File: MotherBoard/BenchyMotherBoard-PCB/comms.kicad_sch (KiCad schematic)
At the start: 9 parts, among them J18 COMMS-PWR, J19 COMMS-ELOAD, J20 COMMS-SWITCHER, J21 RELAYS-CONN, J22 COMMS-LOGIC

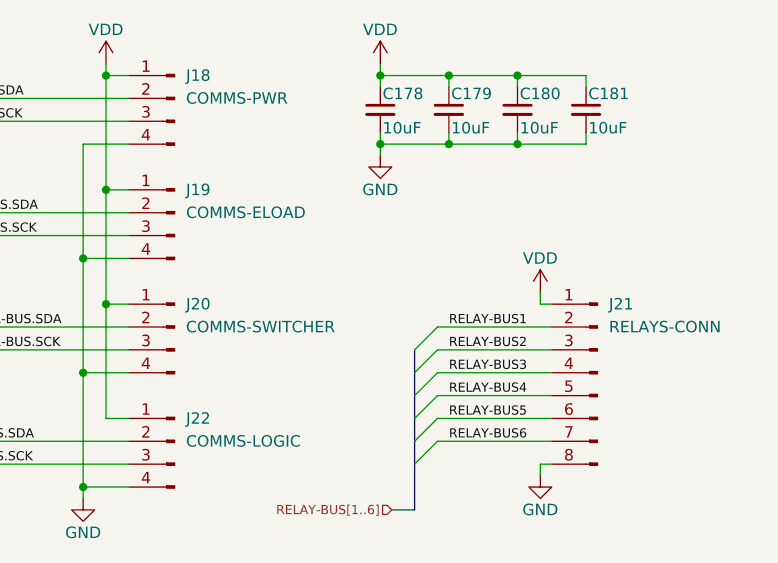
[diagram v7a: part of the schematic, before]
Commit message: Initial DDR routing, start fixing skew
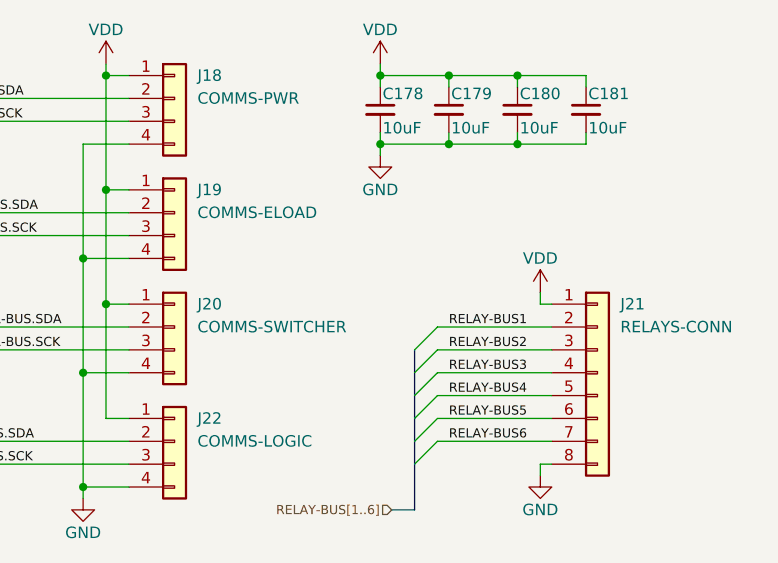
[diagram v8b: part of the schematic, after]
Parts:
- removed J18: COMMS-PWR, Daxxn_Connectors:JST_XH_B4B-XH-A_Vertical, symbol Connector:Conn_01x04_Male
- removed J19: COMMS-ELOAD, Daxxn_Connectors:JST_XH_B4B-XH-A_Vertical, symbol Connector:Conn_01x04_Male
- removed J20: COMMS-SWITCHER, Daxxn_Connectors:JST_XH_B4B-XH-A_Vertical, symbol Connector:Conn_01x04_Male
- removed J21: RELAYS-CONN, Connector_JST:JST_XH_B8B-XH-A_1x08_P2.50mm_Vertical, symbol Connector:Conn_01x08_Male
- removed J22: COMMS-LOGIC, Daxxn_Connectors:JST_XH_B4B-XH-A_Vertical, symbol Connector:Conn_01x04_Male
- added J18: COMMS-PWR, Daxxn_Connectors:JST_XH_B4B-XH-A_Vertical, symbol Connector_Generic:Conn_01x04
- added J19: COMMS-ELOAD, Daxxn_Connectors:JST_XH_B4B-XH-A_Vertical, symbol Connector_Generic:Conn_01x04
- added J20: COMMS-SWITCHER, Daxxn_Connectors:JST_XH_B4B-XH-A_Vertical, symbol Connector_Generic:Conn_01x04
- added J21: RELAYS-CONN, Connector_JST:JST_XH_B8B-XH-A_1x08_P2.50mm_Vertical, symbol Connector_Generic:Conn_01x08
- added J22: COMMS-LOGIC, Daxxn_Connectors:JST_XH_B4B-XH-A_Vertical, symbol Connector_Generic:Conn_01x04
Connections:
- net ELOAD-BUS.SCK: now also J19.3 (Pin_3)
- net ELOAD-BUS.SDA: now also J19.2 (Pin_2)
- net GND: now also J18.4 (Pin_4), J19.4 (Pin_4), J20.4 (Pin_4), J21.8 (Pin_8), J22.4 (Pin_4)
- net LOGIC-BUS.SCK: now also J22.3 (Pin_3)
- net LOGIC-BUS.SDA: now also J22.2 (Pin_2)
- net PWR-BUS.SCK: now also J18.3 (Pin_3)
- net PWR-BUS.SDA: now also J18.2 (Pin_2)
- net RELAY-BUS1: now also J21.2 (Pin_2)
- net RELAY-BUS2: now also J21.3 (Pin_3)
- net RELAY-BUS3: now also J21.4 (Pin_4)
- net RELAY-BUS4: now also J21.5 (Pin_5)
- net RELAY-BUS5: now also J21.6 (Pin_6)
- net RELAY-BUS6: now also J21.7 (Pin_7)
- net SWITCHER-BUS.SCK: now also J20.3 (Pin_3)
- net SWITCHER-BUS.SDA: now also J20.2 (Pin_2)
- net VDD: now also J18.1 (Pin_1), J19.1 (Pin_1), J20.1 (Pin_1), J21.1 (Pin_1), J22.1 (Pin_1)
